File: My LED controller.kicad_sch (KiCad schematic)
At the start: 36 parts, among them J1 AMPHENOL_SPI HDR-20021121-000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, J2 Power SEL, SW3 -, SW4 +, SW5 MODE, SW6 POWER, U1 ESP32-DevKitM-1, U4 SN74AHCT125PWR, U5 AHT20_C2757850, U9 LED_STRIP_CONN

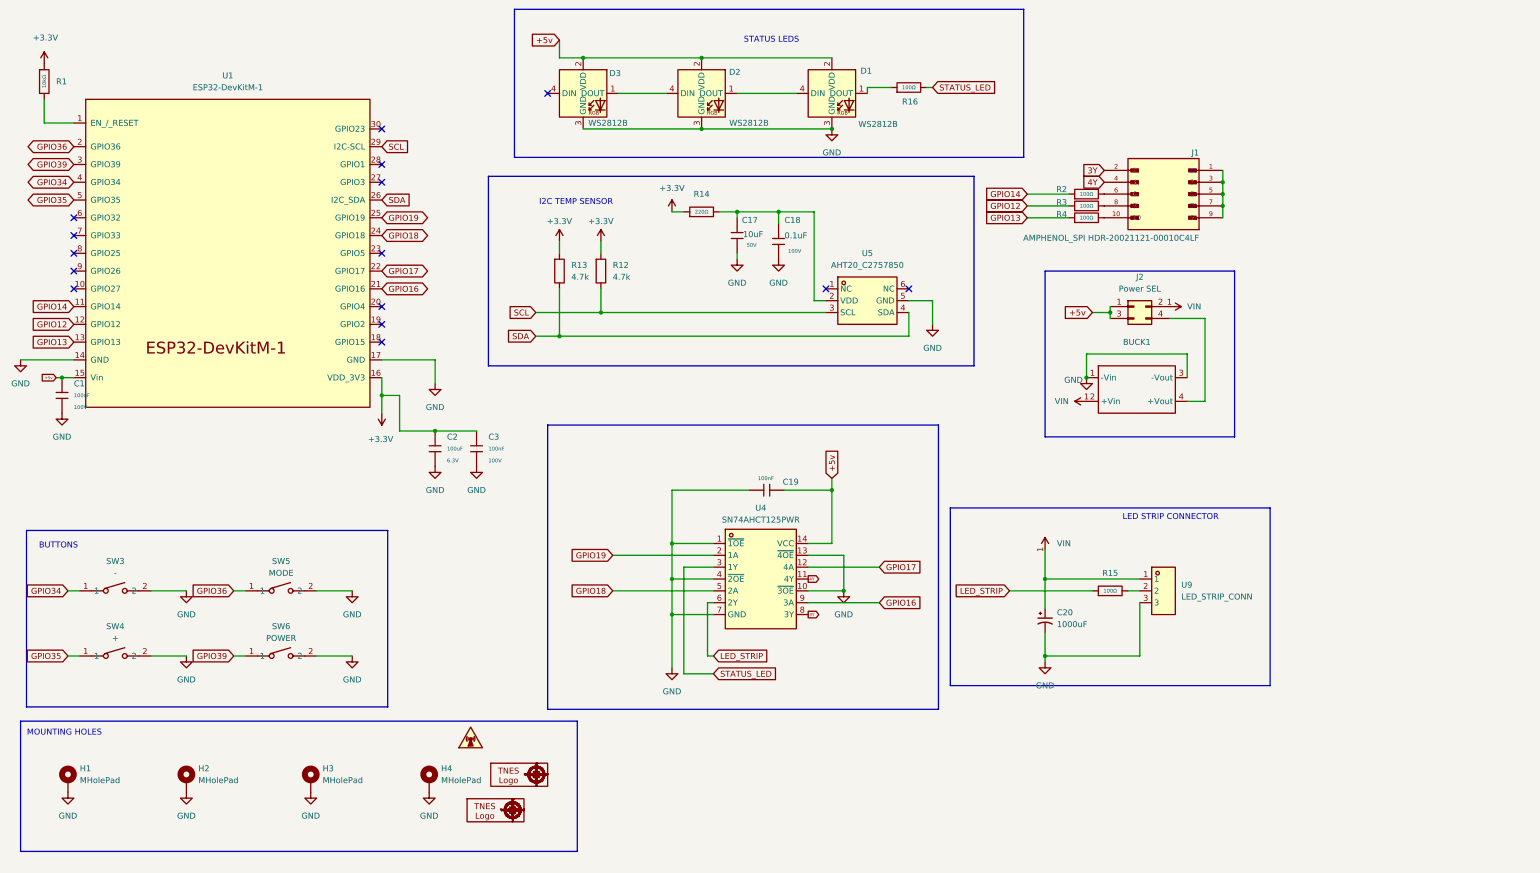
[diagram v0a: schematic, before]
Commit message: Swap Q1 gate bias resistors: R5 100k (to VIN_RAW), R6 10k (to GND) for better PMOS turn-on at 5V input
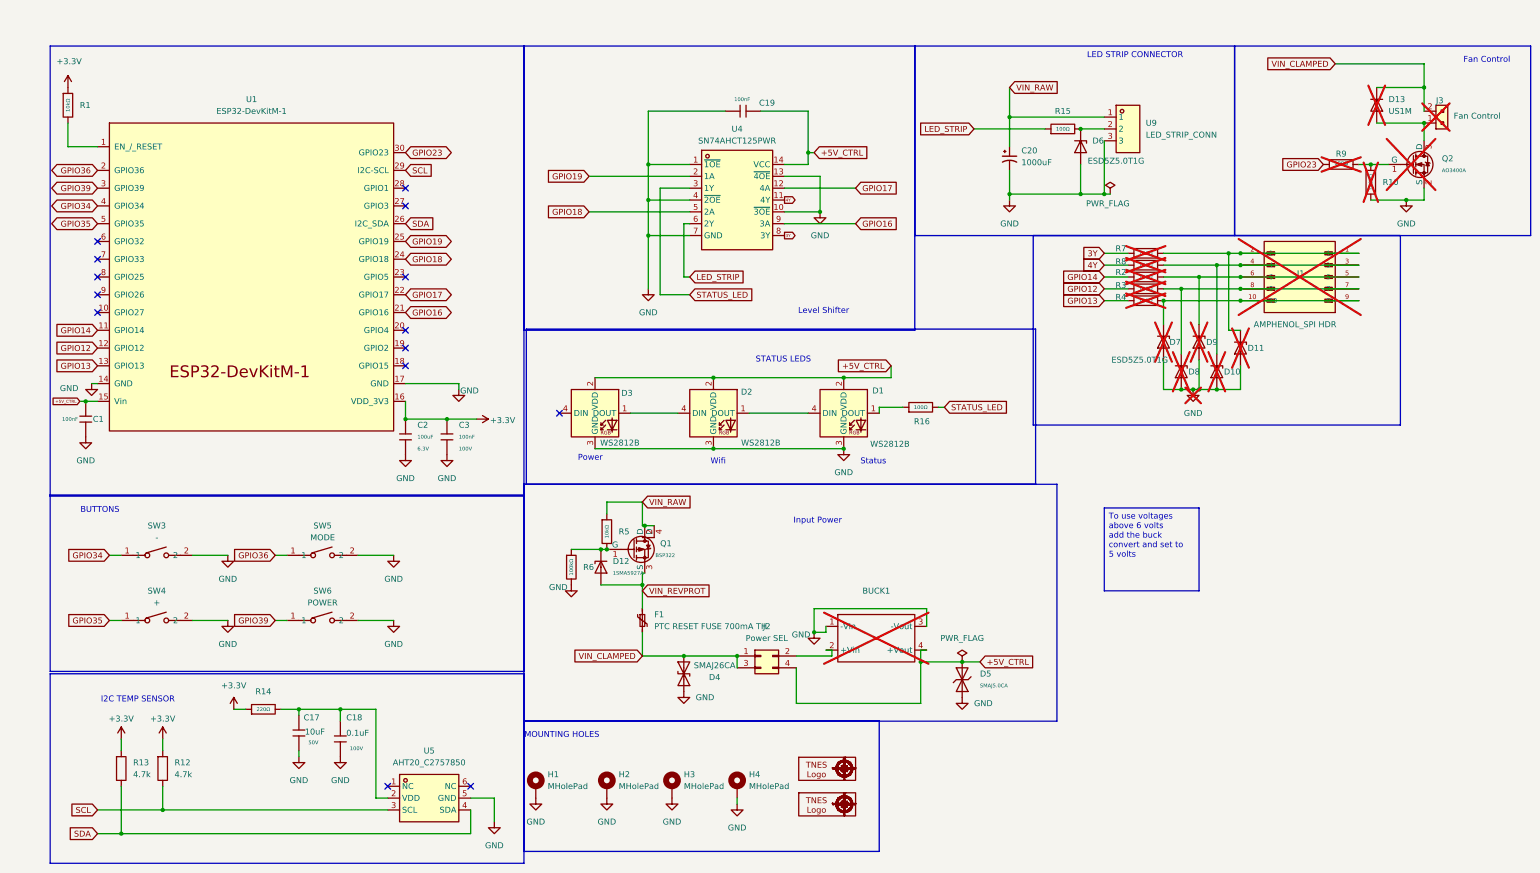
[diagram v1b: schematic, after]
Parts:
- added D10, D11, D6, D7, D8, D9: ESD5Z5.0T1G, Diode_SMD:D_SOD-523, symbol Diode:ESD5Zxx
- added D12: 1SMA5927A, PCM_JLCPCB:D_DO-214AC(SMA), symbol PCM_JLCPCB-Diodes:Zener,1SMA5927A
- added D13: US1M, Diode_SMD:D_SMA, symbol Diode:US1M
- added D4: SMAJ26CA, Diode_SMD:D_SMA, symbol Diode:SMAJ26CA
- added D5: SMAJ5.0CA, PCM_JLCPCB:D_SMA, symbol PCM_JLCPCB-Diodes:TVS-Bi,SMAJ5.0CA
- added F1: PTC RESET FUSE 700mA TH, Fuse:Fuse_Bourns_MF-RHT100, symbol Device:Polyfuse_Small
- added J3: Fan Control, digikey-footprints:PinHeader_1x2_P2.5mm_Drill1.1mm, symbol dk_Rectangular-Connectors-Headers-Male-Pins:B2B-XH-A_LF__SN_
- added Q1: BSP322, PCM_JLCPCB:Q_SOT-23, symbol 1My_Basic components:PMOS,BSP322
- added Q2: AO3400A, PCM_JLCPCB:Q_SOT-23, symbol PCM_JLCPCB-Transistors_1:NMOS,AO3400A
- added R10, R6: 100kΩ, PCM_JLCPCB:R_0805, symbol PCM_JLCPCB-Resistors:0805,100kΩ
- added R5: 10kΩ, PCM_JLCPCB:R_0805, symbol PCM_JLCPCB-Resistors_1:0805,10kΩ
- added R7, R8, R9: 100Ω, PCM_JLCPCB:R_0805, symbol PCM_JLCPCB-Resistors:0805,100Ω
- 10mm1, 10mm2, U1: now left out of the parts list
- BUCK1: now not fitted; now left out of the parts list
- C20: footprint Capacitor_THT:C_Radial_D16.0mm_H25.0mm_P7.50mm -> Capacitor_THT:C_Radial_D10.0mm_H12.5mm_P5.00mm; LCSC Part C383058 -> C398835
- J1: value AMPHENOL_SPI HDR-20021121-00010C4LF -> AMPHENOL_SPI HDR; LCSC (none) -> C150517; now not fitted
- J2: footprint Connector_PinHeader_2.54mm:PinHeader_2x02_P2.54mm_Vertical -> Connector_PinHeader_2.54mm:PinHeader_2x02_P2.54mm_Vertical_SMD; LCSC (none) -> C42163080
- R2, R3, R4: now not fitted
- SW3: LCSC (none) -> C720477; LCSC Part C720477 -> C720477V
- SW4, SW5, SW6: LCSC (none) -> C720477
- U4: LCSC (none) -> C36365
- U5: LCSC (none) -> C2757850
- U9: LCSC (none) -> C474882
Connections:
- net 3Y: now also R7.1; no longer J1.2
- net 4Y: now also R8.1; no longer J1.4
- net GND: now also D10.2 (A), D11.2 (A), D4.1 (A1), D5.1, D6.2 (A), D7.2 (A), D8.2 (A), D9.2 (A), Q2.2 (S), R10.2, R6.2
- net at J1.10, R4.2: now also J1.9, D7.1 (K)
- net at J1.6, R2.2: now also J1.5, D9.1 (K)
- net at J1.8, R3.2: now also J1.7, D8.1 (K)
- net at R15.2, U9.2: now also D6.1 (K)
- net +5V_CTRL: now reaches BUCK1.4 (+Vout), J2.4 (Pin_4)
- net +5V_CTRL: now also C1.1, C19.2, D1.2 (VDD), D2.2 (VDD), D3.2 (VDD), U1.15 (Vin), U4.14 (VCC), D5.2
- net GPIO23: now reaches U1.30 (GPIO23)
- net GPIO23: now also R9.1
- removed net +5v: C1.1, C19.2, D1.2 (VDD), D2.2 (VDD), D3.2 (VDD), J2.1 (Pin_1), J2.3 (Pin_3), U1.15 (Vin), U4.14 (VCC)
- net VIN: no longer names the net of BUCK1.2 (+Vin), J2.2 (Pin_2)
- net VIN: no longer C20.1, U9.1
- new net: D11.1 (K), J1.1, J1.2, R7.2
- new net: D12.1, Q1.1 (G), R5.2, R6.1
- new net: D10.1 (K), J1.3, J1.4, R8.2
- new net: D13.2 (A), J3.1, Q2.3 (D)
- new net: Q2.1 (G), R10.1, R9.2
- new net VIN_CLAMPED: D13.1 (K), D4.2 (A2), F1.2, J2.1 (Pin_1), J2.3 (Pin_3), J3.2
- new net VIN_RAW: C20.1, Q1.2 (D), Q1.4 (D), R5.1, U9.1
- new net VIN_REVPROT: D12.2, F1.1, Q1.3 (S)
- no-connect marks 15 -> 14
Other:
- note added: "Fan Control"
- note added: "Input Power"
- note added: "Level Shifter"
- note added: "Power"
- note added: "Status"
- note added: "Wifi"
- company: (none) -> True North Enterprise Solutions LLC
- title: (none) -> LED Strip Controller 
- moved on the sheet: C1, C17, C18, C19, C2, C20, C3, D1, D2, D3, H1, H2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

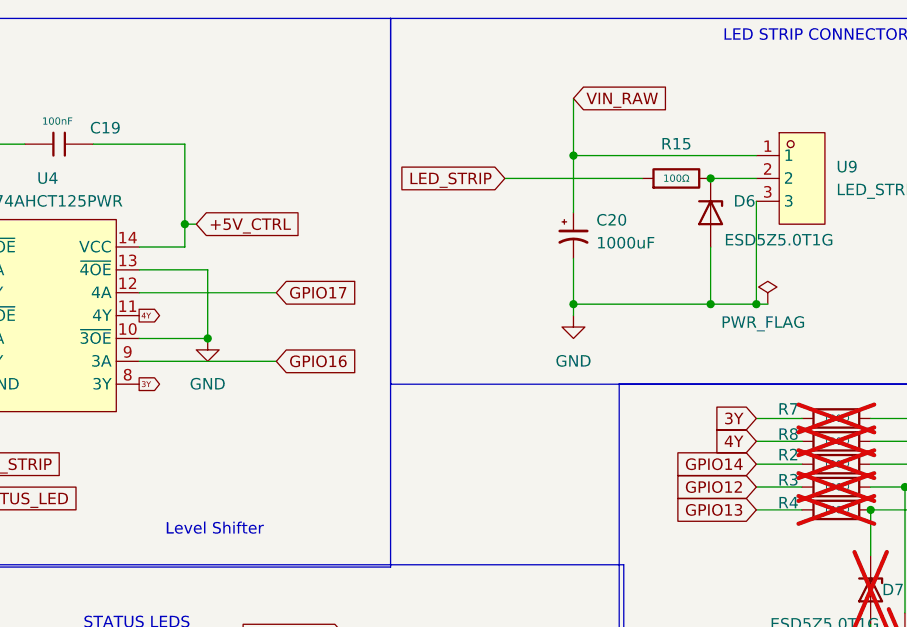
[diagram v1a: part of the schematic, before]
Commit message: Implement pin remap docs and add spare AHCT125 SMT breakout header
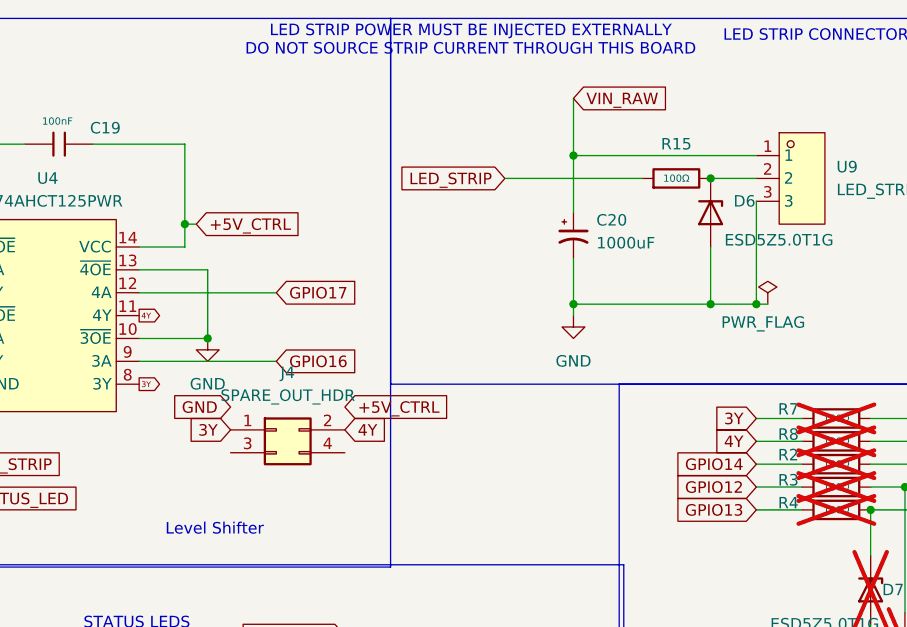
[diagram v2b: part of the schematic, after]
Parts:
- added J4: SPARE_OUT_HDR, Connector_PinHeader_2.54mm:PinHeader_2x02_P2.54mm_Vertical_SMD, symbol Connector_Generic:Conn_02x02_Odd_Even
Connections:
- net 3Y: now also J4.1 (Pin_1)
- net 4Y: now also J4.2 (Pin_2)
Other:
- note added: "LED STRIP POWER MUST BE INJECTED EXTERNALLY DO NOT SOURCE STRIP CURRENT THROUGH THIS BOARD"
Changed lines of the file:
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@@
 		)
 	)
+	(text "LED STRIP POWER MUST BE INJECTED EXTERNALLY\nDO NOT SOURCE STRIP CURRENT THROUGH THIS BOARD"
+		(exclude_from_sim no)
+		(at 214.63 25.4 0)
+		(effects
+			(font
+				(size 1.27 1.27)
+			)
+		)
+	)
 	(text "Level Shifter\n"
 		(exclude_from_sim no)
@@
 		)
 	)
+	(global_label "3Y"
+		(shape input)
+		(at 187.96 68.58 180)
+		(effects
+			(font
+				(size 1.27 1.27)
+			)
+			(justify right)
+		)
+		(property "Intersheetrefs" "${INTERSHEET_REFS}"
+			(at 187.96 68.58 0)
+			(effects
+				(font
+					(size 1.27 1.27)
+				)
+				(hide yes)
+			)
+		)
+	)
+	(global_label "GND"
+		(shape input)
+		(at 187.96 66.04 180)
+		(effects
+			(font
+				(size 1.27 1.27)
+			)
+			(justify right)
+		)
+		(property "Intersheetrefs" "${INTERSHEET_REFS}"
+			(at 187.96 66.04 0)
+			(effects
+				(font
+					(size 1.27 1.27)
+				)
+				(hide yes)
+			)
+		)
+	)
+	(global_label "4Y"
+		(shape input)
+		(at 200.66 68.58 0)
+		(effects
+			(font
+				(size 1.27 1.27)
+			)
+			(justify left)
+		)
+		(property "Intersheetrefs" "${INTERSHEET_REFS}"
+			(at 200.66 68.58 0)
+			(effects
+				(font
+					(size 1.27 1.27)
+				)
+				(hide yes)
+			)
+		)
+	)
+	(global_label "+5V_CTRL"
+		(shape input)
+		(at 200.66 66.04 0)
+		(fields_autoplaced yes)
+		(effects
+			(font
+				(size 1.27 1.27)
+			)
+			(justify left)
+		)
+		(property "Intersheetrefs" "${INTERSHEET_REFS}"
+			(at 213.019 66.04 0)
+			(effects
+				(font
+					(size 1.27 1.27)
+				)
+				(justify left)
+				(hide yes)
+			)
+		)
+	)
 	(global_label "SCL"
 		(shape input)
@@
 					(unit 1)
 				)
+			)
+		)
+	)
+	(symbol
+		(lib_id "Connector_Generic:Conn_02x02_Odd_Even")
+		(at 193.04 68.58 0)
+		(unit 1)
+		(exclude_from_sim no)
+		(in_bom yes)
+		(on_board yes)
+		(dnp no)
+		(fields_autoplaced yes)
+		(property "Reference" "J4"
+			(at 194.31 62.23 0)
+			(effects
+				(font
+					(size 1.27 1.27)
+				)
+			)
+		)
+		(property "Value" "SPARE_OUT_HDR"
+			(at 194.31 64.77 0)
+			(effects
+				(font
+					(size 1.27 1.27)
+				)
+			)
+		)
+		(property "Footprint" "Connector_PinHeader_2.54mm:PinHeader_2x02_P2.54mm_Vertical_SMD"
+			(at 193.04 68.58 0)
+			(effects
+				(font
+					(size 1.27 1.27)
+				)
+				(hide yes)
+			)
+		)
+		(property "Datasheet" "~https://www.lcsc.com/datasheet/C42163080.pdf?spm=wm.sxq.inf.ggs___wm.fly.bg.4.xh&lcsc_vid=RlhYUFQHTlkIAlRTQQQMVwYCQQNeBlcDQQIMXlRfE1cxVlNeR1VZUFNQRFJfVTsOAxUeFF5JWBYZEEoKFBINSQcJGk4eFQsCAgIaSgADAwAHC0slQ1ZdUlFQQlZADxALGw%3D%3D"
+			(at 193.04 68.58 0)
+			(effects
+				(font
+					(size 1.27 1.27)
+				)
+				(hide yes)
+			)
+		)
+		(property "Description" "CONN HEADER 4POS 2.54mm DUAL ROW SMD"
+			(at 193.04 68.58 0)
+			(effects
+				(font
+					(size 1.27 1.27)
+				)
+				(hide yes)
+			)
+		)
+		(property "LCSC" "C42163080"
+			(at 193.04 68.58 0)
+			(effects
+				(font
+					(size 1.27 1.27)
+				)
+				(hide yes)
+			)
+		)
+		(pin "4"
+		)
+		(pin "3"
+		)
+		(pin "2"
+		)
+		(pin "1"
+		)
+		(instances
+			(project "My LED controller"
+				(path "/00777be0-2c66-4893-8910-2bcda97b7c36"
+					(reference "J4")
+					(unit 1)
+				)

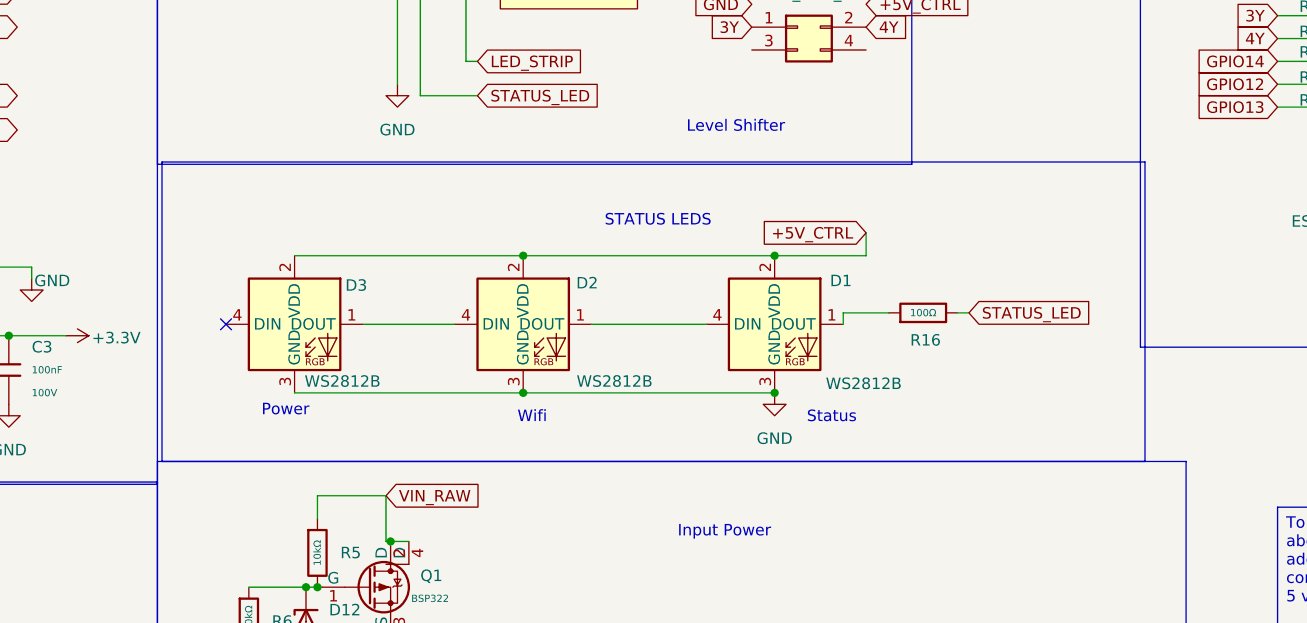
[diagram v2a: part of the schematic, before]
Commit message: Schematic: mirror WS2812 symbols and adjust annotation placement
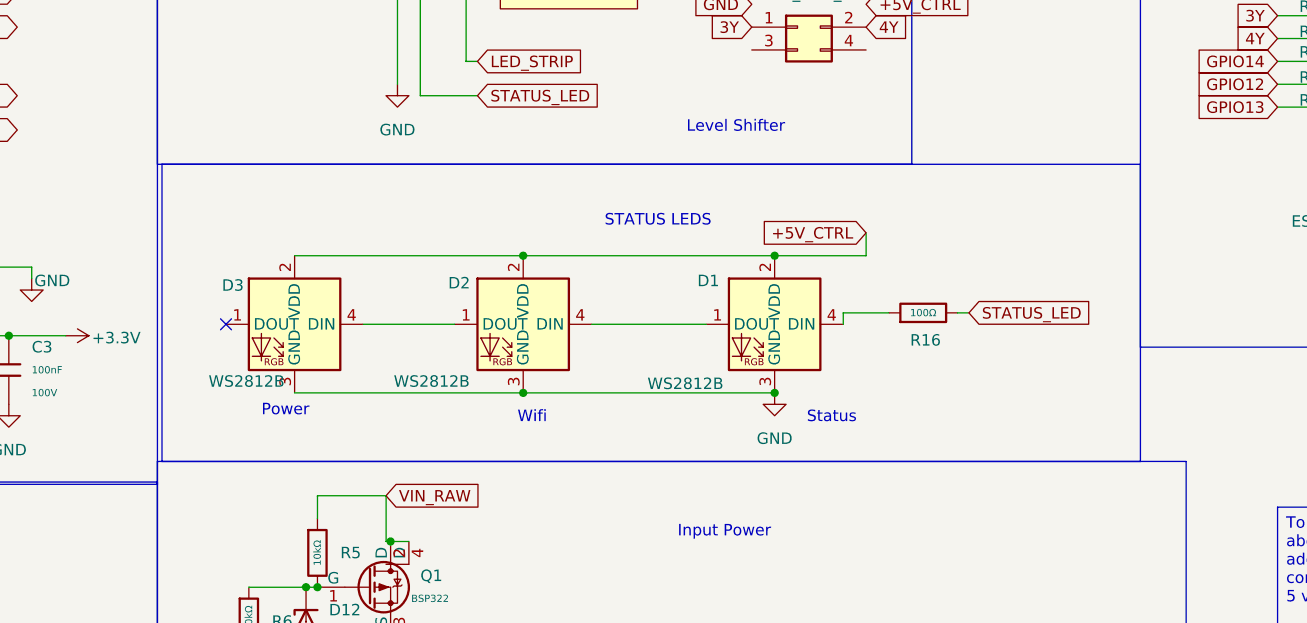
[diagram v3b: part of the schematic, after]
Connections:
- net at D3.1 (DOUT): no longer D2.4 (DIN)
- net at D3.4 (DIN): now also D2.1 (DOUT)
- net at D1.4 (DIN): now also R16.1; no longer D2.1 (DOUT)
- net at D1.1 (DOUT): now also D2.4 (DIN); no longer R16.1
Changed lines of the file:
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@@
 	)
 	(rectangle
-		(start 122.428 83.566)
-		(end 231.648 116.84)
+		(start 122.428 83.82)
+		(end 231.14 116.84)
 		(stroke
 			(width 0)
@@
 		(lib_id "PCM_JLCPCB-Extended:LED, WS2812B, 1615")
 		(at 137.16 101.6 0)
+		(mirror y)
 		(unit 1)
 		(exclude_from_sim no)
@@
 		(dnp no)
 		(property "Reference" "D3"
-			(at 144.018 97.282 0)
+			(at 130.302 97.282 0)
 			(effects
 				(font
@@
 		)
 		(property "Value" "WS2812B"
-			(at 142.494 107.95 0)
+			(at 131.826 107.95 0)
 			(effects
 				(font
@@
 		)
 		(property "Datasheet" "https://atta.szlcsc.com/upload/public/pdf/source/20230111/5AD58278EBED6B6650A81C53A19BF314.pdf"
-			(at 134.874 101.473 0)
+			(at 139.446 101.473 0)
 			(effects
 				(font
@@
 		(lib_id "PCM_JLCPCB-Extended:LED, WS2812B, 1615")
 		(at 162.56 101.6 0)
+		(mirror y)
 		(unit 1)
 		(exclude_from_sim no)
@@
 		(dnp no)
 		(property "Reference" "D2"
-			(at 169.672 97.028 0)
+			(at 155.448 97.028 0)
 			(effects
 				(font
@@
 		)
 		(property "Value" "WS2812B"
-			(at 172.72 107.95 0)
+			(at 152.4 107.95 0)
 			(effects
 				(font
@@
 		)
 		(property "Datasheet" "https://atta.szlcsc.com/upload/public/pdf/source/20230111/5AD58278EBED6B6650A81C53A19BF314.pdf"
-			(at 160.274 101.473 0)
+			(at 164.846 101.473 0)
 			(effects
 				(font
@@
 		(lib_id "PCM_JLCPCB-Extended:LED, WS2812B, 1615")
 		(at 190.5 101.6 0)
+		(mirror y)
 		(unit 1)
 		(exclude_from_sim no)
@@
 		(dnp no)
 		(property "Reference" "D1"
-			(at 197.866 96.774 0)
+			(at 183.134 96.774 0)
 			(effects
 				(font
@@
 		)
 		(property "Value" "WS2812B"
-			(at 200.406 108.204 0)
+			(at 180.594 108.204 0)
 			(effects
 				(font
@@
 		)
 		(property "Datasheet" "https://atta.szlcsc.com/upload/public/pdf/source/20230111/5AD58278EBED6B6650A81C53A19BF314.pdf"
-			(at 188.214 101.473 0)
+			(at 192.786 101.473 0)
 			(effects
 				(font
